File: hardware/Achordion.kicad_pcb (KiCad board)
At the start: 2 copper layers, 44.5 x 109.4 mm, 96 parts, among them J1 Power, J10 Jack, J11 Jack, J4 Jack, J5 Jack, J6 Jack, J7 Jack, J8 Jack, J9 Jack, SW2 Button, U4 LM4040C10, U6 TL072, U7 MCP6002, U8 MCP6002, U9 MCP6002

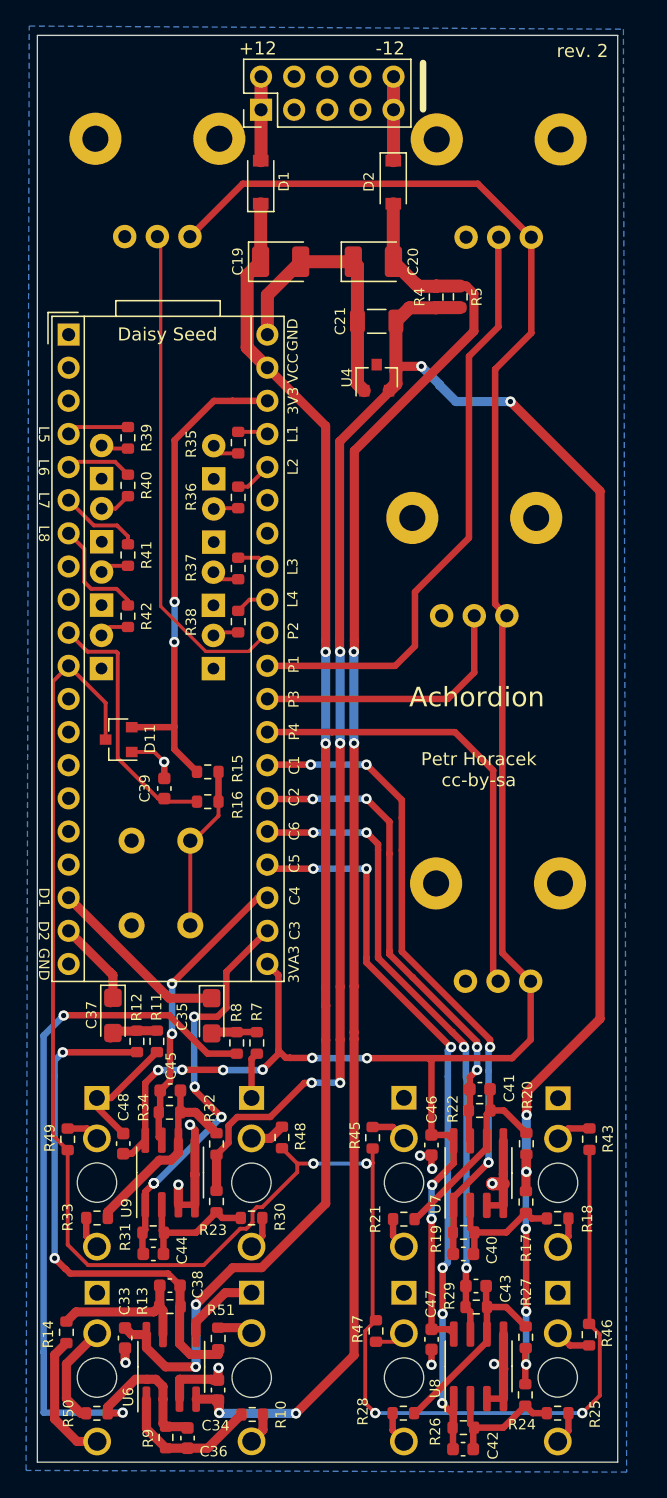
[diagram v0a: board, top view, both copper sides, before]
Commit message: Use bigger pads in PCB
Make hand soldering easier.

Signed-off-by: Petr Horacek <hrck@protonmail.com>
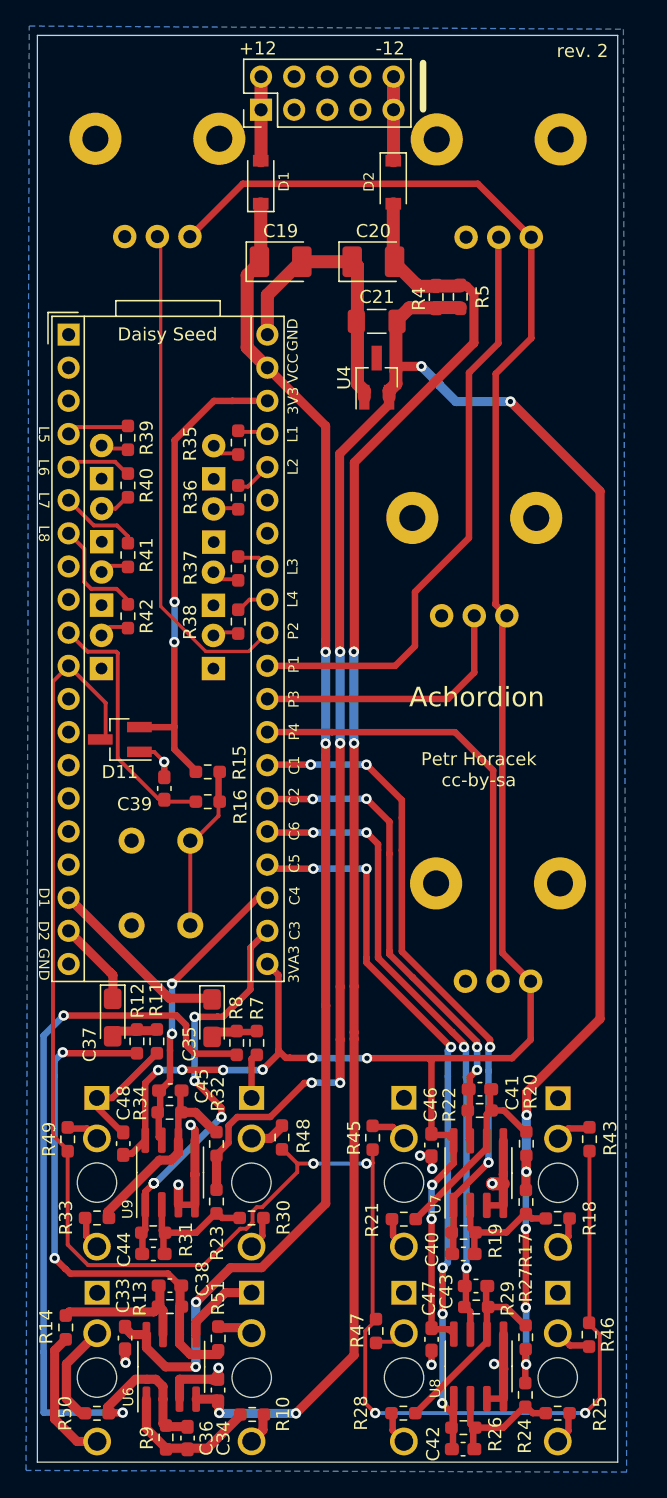
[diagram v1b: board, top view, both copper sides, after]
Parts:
- C19, C20: footprint Capacitor_Tantalum_SMD:CP_EIA-3528-21_Kemet-B -> Capacitor_Tantalum_SMD:CP_EIA-3528-21_Kemet-B_Pad1.50x2.35mm_HandSolder
- C21: footprint Capacitor_SMD:C_1206_3216Metric -> Capacitor_SMD:C_1206_3216Metric_Pad1.33x1.80mm_HandSolder
- C33, C34, C36, C38, C39, C40, C41, C42, C43, C44, C45, C46, C47, C48: footprint Capacitor_SMD:C_0603_1608Metric -> Capacitor_SMD:C_0603_1608Metric_Pad1.08x0.95mm_HandSolder
- C35, C37: footprint Capacitor_Tantalum_SMD:CP_EIA-3216-18_Kemet-A -> Capacitor_Tantalum_SMD:CP_EIA-3216-18_Kemet-A_Pad1.58x1.35mm_HandSolder
- D11, U4: footprint Package_TO_SOT_SMD:SOT-23 -> Package_TO_SOT_SMD:SOT-23_Handsoldering
- R10, R11, R12, R13, R14, R15, R16, R17, R18, R19, R20, R21, R22, R23, R24, R25, R26, R27, R28, R29, R30, R31, R32, R33, R34, R35, R36, R37, R38, R39, R4, R40, R41, R42, R43, R45, R46, R47, R48, R49, R5, R50, R51, R7, R8, R9: footprint Resistor_SMD:R_0603_1608Metric -> Resistor_SMD:R_0603_1608Metric_Pad0.98x0.95mm_HandSolder
- moved R14 0.38 mm to (125.0, 140.6)
- moved C35 0.18 mm to (136.2, 116.9)
- moved C37 0.16 mm to (128.6, 116.9)
- moved D11 0.09 mm to (129.2, 95.6)
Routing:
- net GND: track 77.3 -> 78.5 mm
- net Net-(C36-Pad2): track 63.5 -> 64.5 mm

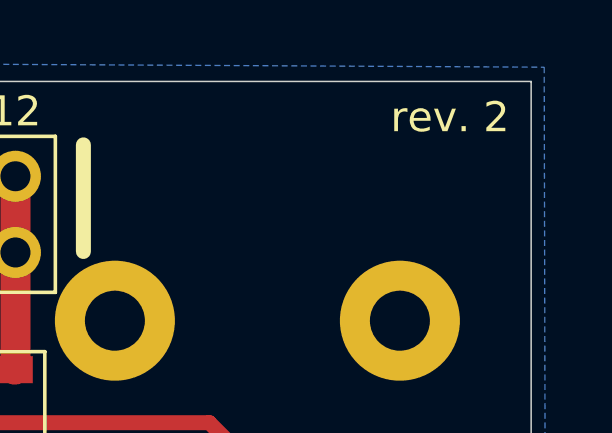
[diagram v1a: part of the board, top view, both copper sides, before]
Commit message: Mark revision 3
Revision 2 was already sent to be printed. Since then, pad sizes were
changed.

Signed-off-by: Petr Horacek <hrck@protonmail.com>
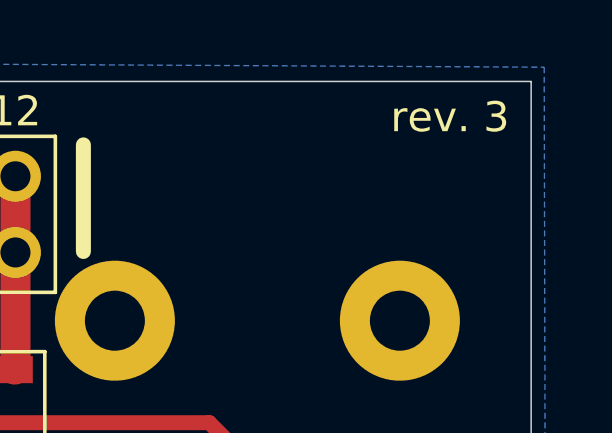
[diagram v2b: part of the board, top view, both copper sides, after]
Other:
- board text added: "rev. 3"
- board text removed: "rev. 2"
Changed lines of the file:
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@@
     (title Achordion)
     (date 2021-04-25)
-    (rev 2)
+    (rev 3)
     (company "Petr Horáček")
     (comment 1 hrck@protonmail.com)
@@
       (effects (font (size 1 1) (thickness 0.15)))
     )
+    (fp_line (start 1.65 0.73) (end -1.65 0.73) (layer F.CrtYd) (width 0.05))
+    (fp_line (start 1.65 -0.73) (end 1.65 0.73) (layer F.CrtYd) (width 0.05))
+    (fp_line (start -1.65 -0.73) (end 1.65 -0.73) (layer F.CrtYd) (width 0.05))
+    (fp_line (start -1.65 0.73) (end -1.65 -0.73) (layer F.CrtYd) (width 0.05))
+    (fp_line (start -0.254724 0.5225) (end 0.254724 0.5225) (layer F.SilkS) (width 0.12))
+    (fp_line (start -0.254724 -0.5225) (end 0.254724 -0.5225) (layer F.SilkS) (width 0.12))
+    (fp_line (start 0.8 0.4125) (end -0.8 0.4125) (layer F.Fab) (width 0.1))
+    (fp_line (start 0.8 -0.4125) (end 0.8 0.4125) (layer F.Fab) (width 0.1))
+    (fp_line (start -0.8 -0.4125) (end 0.8 -0.4125) (layer F.Fab) (width 0.1))
+    (fp_line (start -0.8 0.4125) (end -0.8 -0.4125) (layer F.Fab) (width 0.1))
     (fp_text user %R (at 0 0 90) (layer F.Fab)
       (effects (font (size 0.4 0.4) (thickness 0.06)))
     )
-    (fp_line (start -0.8 0.4125) (end -0.8 -0.4125) (layer F.Fab) (width 0.1))
-    (fp_line (start -0.8 -0.4125) (end 0.8 -0.4125) (layer F.Fab) (width 0.1))
-    (fp_line (start 0.8 -0.4125) (end 0.8 0.4125) (layer F.Fab) (width 0.1))
-    (fp_line (start 0.8 0.4125) (end -0.8 0.4125) (layer F.Fab) (width 0.1))
-    (fp_line (start -0.254724 -0.5225) (end 0.254724 -0.5225) (layer F.SilkS) (width 0.12))
-    (fp_line (start -0.254724 0.5225) (end 0.254724 0.5225) (layer F.SilkS) (width 0.12))
-    (fp_line (start -1.65 0.73) (end -1.65 -0.73) (layer F.CrtYd) (width 0.05))
-    (fp_line (start -1.65 -0.73) (end 1.65 -0.73) (layer F.CrtYd) (width 0.05))
-    (fp_line (start 1.65 -0.73) (end 1.65 0.73) (layer F.CrtYd) (width 0.05))
-    (fp_line (start 1.65 0.73) (end -1.65 0.73) (layer F.CrtYd) (width 0.05))
-    (pad 2 smd roundrect (at 0.9125 0 270) (size 0.975 0.95) (layers F.Cu F.Paste F.Mask) (roundrect_rratio 0.25)
-      (net 16 "Net-(C42-Pad2)"))
     (pad 1 smd roundrect (at -0.9125 0 270) (size 0.975 0.95) (layers F.Cu F.Paste F.Mask) (roundrect_rratio 0.25)
       (net 6 -10V))
+    (pad 2 smd roundrect (at 0.9125 0 270) (size 0.975 0.95) (layers F.Cu F.Paste F.Mask) (roundrect_rratio 0.25)
+      (net 16 "Net-(C42-Pad2)"))
     (model ${KISYS3DMOD}/Resistor_SMD.3dshapes/R_0603_1608Metric.wrl
       (at (xyz 0 0 0))
@@
   (gr_circle (center 162.726001 144.48) (end 164.237002 144.48) (layer Edge.Cuts) (width 0.1))
   (gr_circle (center 139.236001 129.55) (end 140.747002 129.55) (layer Edge.Cuts) (width 0.1))
-  (gr_text "rev. 2" (at 164.62 42.77) (layer F.SilkS)
+  (gr_text "rev. 3" (at 164.62 42.77) (layer F.SilkS)
     (effects (font (size 1 1) (thickness 0.15)))
   )

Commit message: Release version 0.2.0
Signed-off-by: Petr Horacek <hrck@protonmail.com>
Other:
- board text added: "board v0.2.0"
- board text removed: "rev. 3"

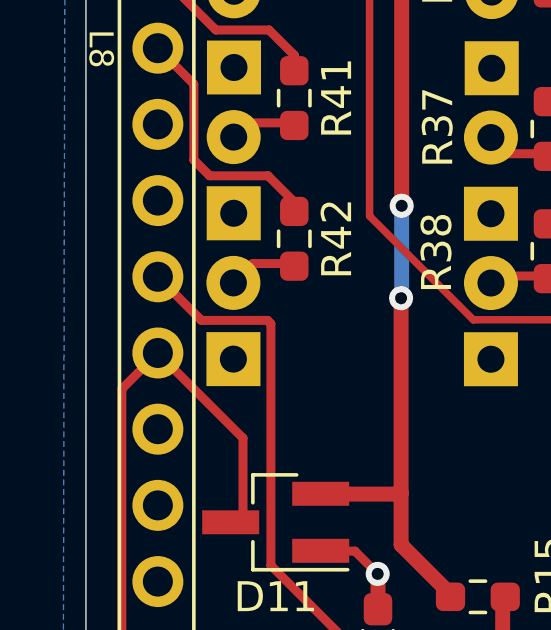
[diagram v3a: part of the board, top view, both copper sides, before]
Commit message: Label button and probe pins on PCB
Signed-off-by: Petr Horacek <hrck@protonmail.com>
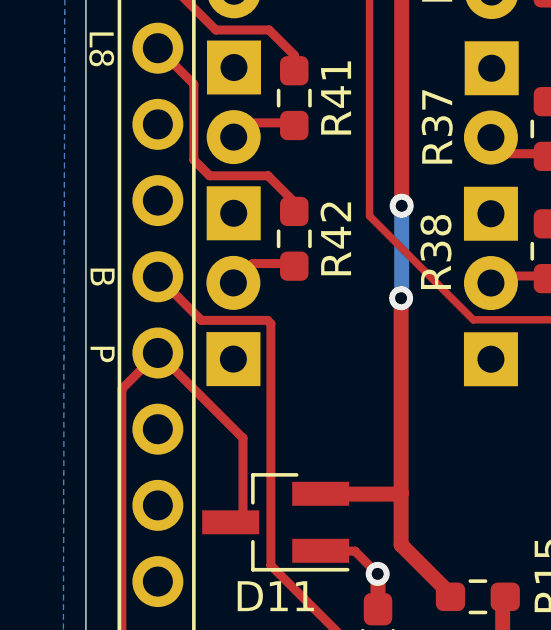
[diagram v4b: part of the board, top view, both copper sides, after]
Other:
- board text added: "B"
- board text added: "P"

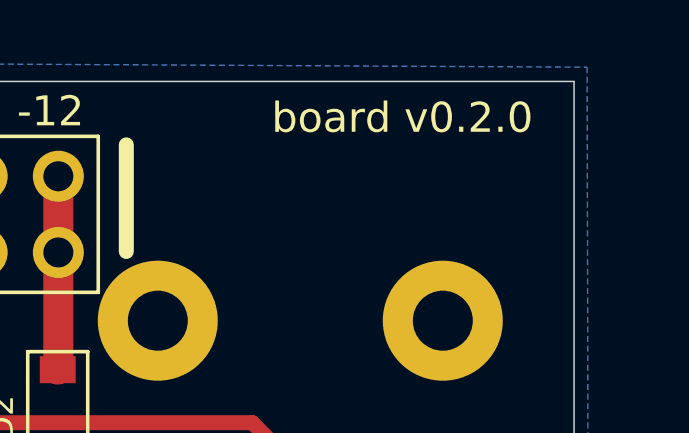
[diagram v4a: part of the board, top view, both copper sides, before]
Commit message: Release version 0.3.0
* Detune sections now respond logarithmically, this allows for finer
  control in lower values.
* Added pulse waveforms of variable width.
* Support multiple wavetable banks.
* Label button and probe pins on the PCB.
* Switch to Daisy Seed, STM32H7.

Signed-off-by: Petr Horacek <hrck@protonmail.com>
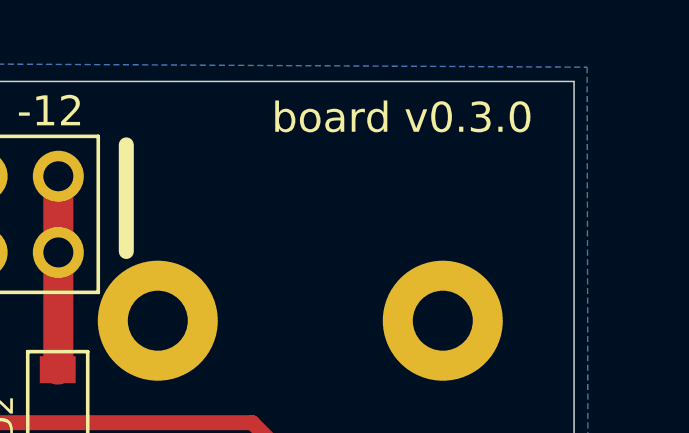
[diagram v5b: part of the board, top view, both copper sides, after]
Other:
- board text added: "board v0.3.0"
- board text removed: "board v0.2.0"
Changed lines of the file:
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@@
   (gr_circle (center 162.726001 144.48) (end 164.237002 144.48) (layer Edge.Cuts) (width 0.1))
   (gr_circle (center 139.236001 129.55) (end 140.747002 129.55) (layer Edge.Cuts) (width 0.1))
-  (gr_text "board v0.2.0" (at 157.24 42.79) (layer F.SilkS)
+  (gr_text "board v0.3.0" (at 157.24 42.79) (layer F.SilkS)
     (effects (font (size 1 1) (thickness 0.15)) (justify left))
   )

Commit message: Release version 0.4.0
* Allowed control of all parameters through CV:
  - Root note, adhering to V/OCT. When connected, Note potentiometer controls
    octave offset.
  - Wavetable position. When connected, Wavetable potentiometer controls the
    offset.
  - Chord. When connected, Chord potentiometer controls the offset.
  - Detune. When connected, Detune potentiometer controls the offset.
  - Scale mode.
  - Scale root note, adhering to V/OCT.
* Fixed the bug where root and chord went to both channels.
* Introduced fade in when the module is powered on.
* Fixed an issue where full detune setting would disable detune.

Signed-off-by: Petr Horacek <hrck@protonmail.com>
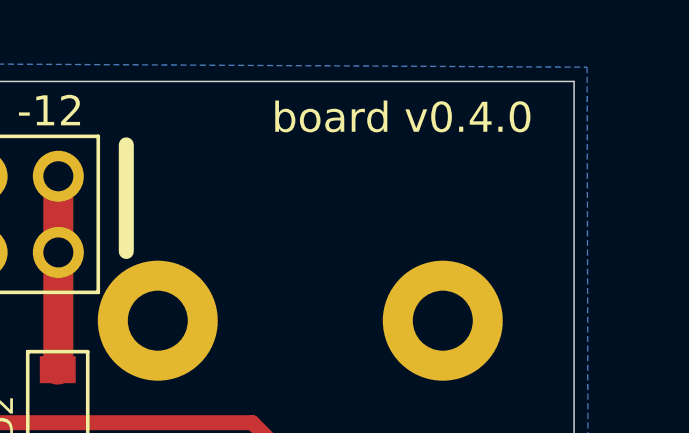
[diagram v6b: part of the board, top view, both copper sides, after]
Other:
- board text added: "board v0.4.0"
- board text removed: "board v0.3.0"
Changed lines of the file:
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@@
   (gr_circle (center 162.726001 144.48) (end 164.237002 144.48) (layer Edge.Cuts) (width 0.1))
   (gr_circle (center 139.236001 129.55) (end 140.747002 129.55) (layer Edge.Cuts) (width 0.1))
-  (gr_text "board v0.3.0" (at 157.24 42.79) (layer F.SilkS)
+  (gr_text "board v0.4.0" (at 157.24 42.79) (layer F.SilkS)
     (effects (font (size 1 1) (thickness 0.15)) (justify left))
   )

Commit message: Release version 0.5.0
* Allow control of wavetable bank through Wavetable pot while holding the
  button.
* Allow control of scale root through Note pot while holding the button. This
  value will be combined with the Tonic CV in case it is connected.
* Allow control of scale mode through Chord pot while holding the button. This
  value will be combined with the Mode CV in case it is connected.
* Remove support for 4 degrees of chords. It draws too much resources.

Signed-off-by: Petr Horacek <hrck@protonmail.com>
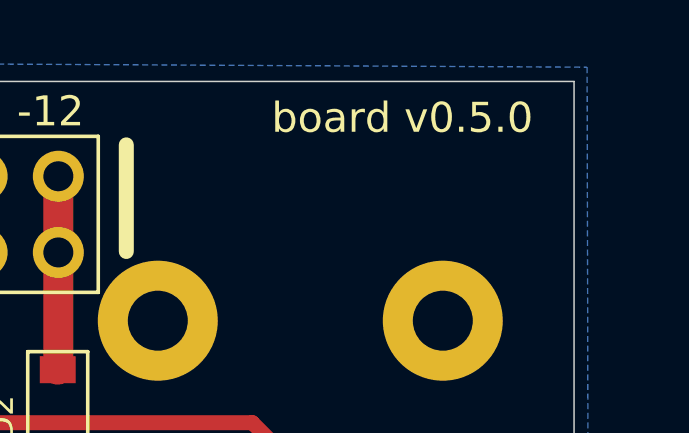
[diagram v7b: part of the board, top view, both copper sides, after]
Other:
- board text added: "board v0.5.0"
- board text removed: "board v0.4.0"
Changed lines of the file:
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@@
   (gr_circle (center 162.726001 144.48) (end 164.237002 144.48) (layer Edge.Cuts) (width 0.1))
   (gr_circle (center 139.236001 129.55) (end 140.747002 129.55) (layer Edge.Cuts) (width 0.1))
-  (gr_text "board v0.4.0" (at 157.24 42.79) (layer F.SilkS)
+  (gr_text "board v0.5.0" (at 157.24 42.79) (layer F.SilkS)
     (effects (font (size 1 1) (thickness 0.15)) (justify left))
   )

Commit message: Release version 0.6.0
* Added tooling supporting generation of wavetables from raw audio.
* Lowered LPF on wavetables to make the lower end thicker.
* Use floats for audio buffers instead of u16.
* Remove pulse wavetable bank.
* Add a bank compiled of FM, distorted and sampled wavetables.
* Add a bank compiled of soft wavetables.
* Add a bank of vocal wavetables.

Signed-off-by: Petr Horacek <hrck@protonmail.com>
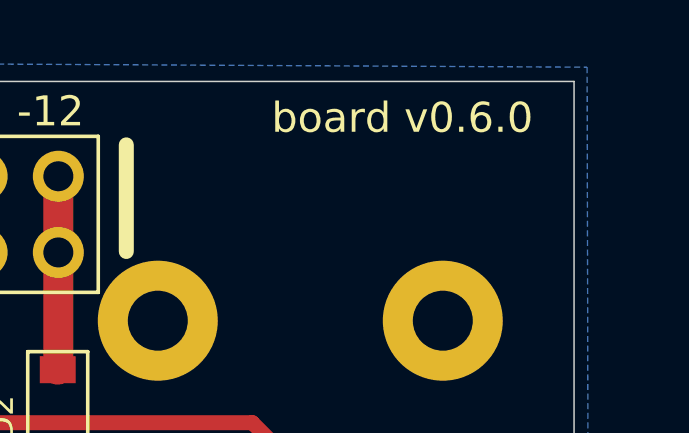
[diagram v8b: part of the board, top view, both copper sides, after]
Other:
- board text added: "board v0.6.0"
- board text removed: "board v0.5.0"
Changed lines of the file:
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@@
   (gr_circle (center 162.726001 144.48) (end 164.237002 144.48) (layer Edge.Cuts) (width 0.1))
   (gr_circle (center 139.236001 129.55) (end 140.747002 129.55) (layer Edge.Cuts) (width 0.1))
-  (gr_text "board v0.5.0" (at 157.24 42.79) (layer F.SilkS)
+  (gr_text "board v0.6.0" (at 157.24 42.79) (layer F.SilkS)
     (effects (font (size 1 1) (thickness 0.15)) (justify left))
   )
